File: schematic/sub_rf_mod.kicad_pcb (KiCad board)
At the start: 2 copper layers, 70.1 x 50.4 mm, 72 parts, among them J1 Conn_01x08, J2 MD-90SM, Q1 2N3906, U1 NE5532, U2 MAX4395ESD, U3 LM1881, U5 ADG453, U6 LMH1251, U7 MAX4395ESD, U8 L7805

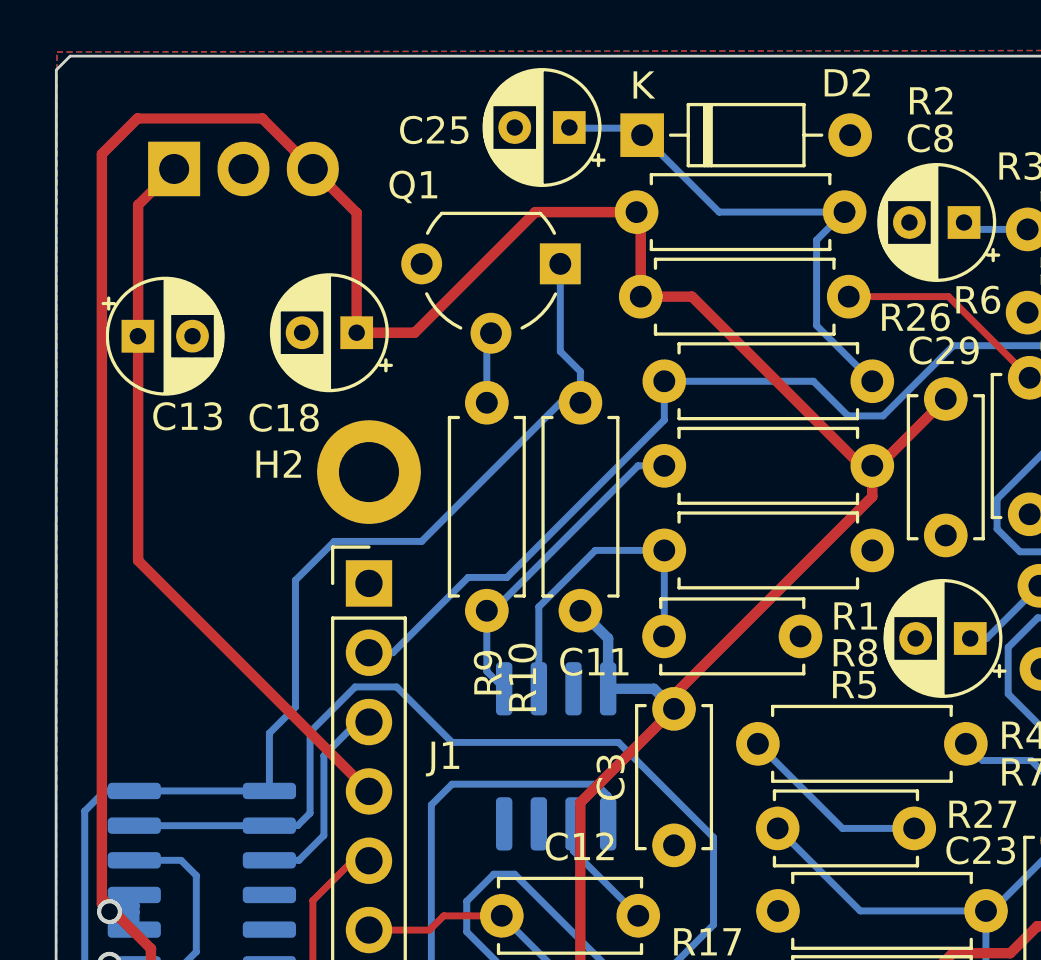
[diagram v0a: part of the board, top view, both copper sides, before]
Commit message: add schematic
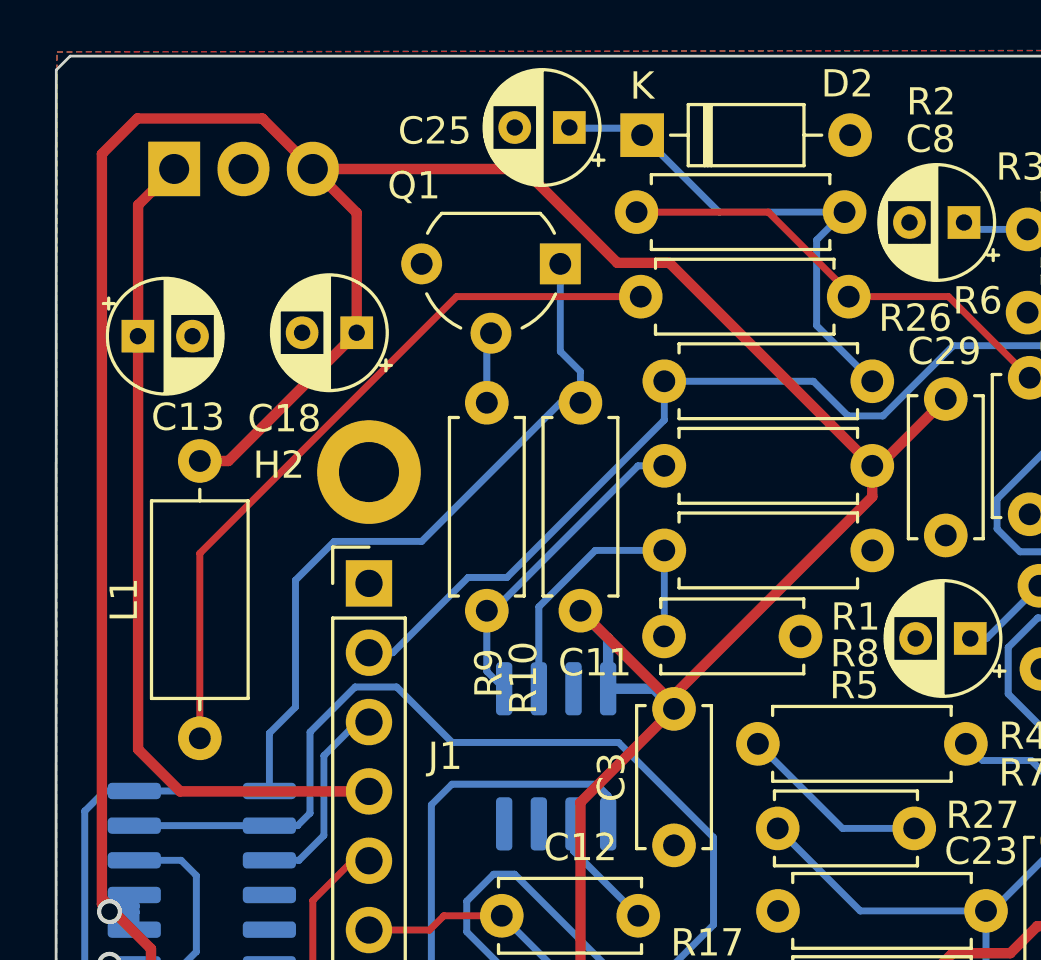
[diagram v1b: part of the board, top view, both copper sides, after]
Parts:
- added L1: 4.7uH, Inductor_THT:L_Axial_L7.0mm_D3.3mm_P10.16mm_Horizontal_Fastron_MICC, F.Cu at (107.6, 78.3)
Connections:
- C2 pad 2: Net-(U1C-V+) -> +5VA
- R2 pad 2: +5VD -> +5VA
- R26 pad 1: Net-(U1C-V+) -> +5VA
- R26 pad 2: +5VD -> Net-(L1-Pad1)
- U1 pad 8: Net-(U1C-V+) -> +5VA
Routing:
- net Net-(L1-Pad1): track 0.00 -> 26.8 mm
- net +5VA: track 0.00 -> 20.0 mm
- net +5VD: track 234.9 -> 246.3 mm
- net Net-(U1C-V+): track 10.9 -> 0.00 mm
- net VDDF: track 26.9 -> 30.9 mm
